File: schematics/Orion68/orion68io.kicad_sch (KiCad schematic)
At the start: 48 parts, among them IC4 XR68C681CJTR-F, J1 LevelConverter, J200 Euro96pin, J22 Kbd_usb, J23 Conn_01x06, Q4 14.7456MHz, U200 GAL16V8, U25 SN74LVC245APW, U26 SN74LVC245APW, U27 RP5C01A, U30 LM2937xT, U33 68681, Y3 Crystal

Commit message: Now picoMultiIO read usb and ps2 keyboards
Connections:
- net CS_SDCARD: now also U_S200.29 (GP22); no longer U_S200.27 (GP21)
- net TX: now reaches U_S200.26 (GP20)
- new net RX: U_S200.27 (GP21)
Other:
- moved on the sheet: J22
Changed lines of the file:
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@@
 	(wire
 		(pts
-			(xy 77.47 140.97) (xy 77.47 143.51)
+			(xy 246.38 100.33) (xy 246.38 102.87)
 		)
 		(stroke
@@
 	(wire
 		(pts
-			(xy 77.47 130.81) (xy 80.01 130.81)
+			(xy 246.38 90.17) (xy 248.92 90.17)
 		)
 		(stroke
@@
 	(wire
 		(pts
-			(xy 77.47 128.27) (xy 77.47 130.81)
+			(xy 246.38 87.63) (xy 246.38 90.17)
 		)
 		(stroke
@@
 	(wire
 		(pts
-			(xy 77.47 140.97) (xy 80.01 140.97)
+			(xy 246.38 100.33) (xy 248.92 100.33)
 		)
 		(stroke
@@
 		)
 	)
+	(label "RX"
+		(at 227.33 133.35 0)
+		(effects
+			(font
+				(size 1.27 1.27)
+			)
+			(justify left bottom)
+		)
+	)
 	(label "A20"
 		(at 391.16 59.69 0)
@@
 		)
 	)
+	(label "TX"
+		(at 227.33 135.89 0)
+		(effects
+			(font
+				(size 1.27 1.27)
+			)
+			(justify left bottom)
+		)
+	)
 	(label "{slash}DTACK_68681"
 		(at 364.49 124.46 180)
@@
 	)
 	(label "TXDA"
-		(at 80.01 138.43 180)
+		(at 248.92 97.79 180)
 		(effects
 			(font
@@
 	)
 	(label "CS_SDCARD"
-		(at 227.33 133.35 0)
+		(at 227.33 130.81 0)
 		(effects
 			(font
@@
 	)
 	(label "RXDA"
-		(at 80.01 135.89 180)
+		(at 248.92 95.25 180)
 		(effects
 			(font
@@
 	(symbol
 		(lib_id "Connector_Generic:Conn_01x05")
-		(at 85.09 135.89 0)
+		(at 254 95.25 0)
 		(unit 1)
 		(exclude_from_sim no)
@@
 		(fields_autoplaced yes)
 		(property "Reference" "J22"
-			(at 87.63 134.6199 0)
+			(at 256.54 93.9799 0)
 			(effects
 				(font
@@
 		)
 		(property "Value" "Kbd_usb"
-			(at 87.63 137.1599 0)
+			(at 256.54 96.5199 0)
 			(effects
 				(font
@@
 		)
 		(property "Footprint" ""
-			(at 85.09 135.89 0)
+			(at 254 95.25 0)
 			(effects
 				(font
@@
 		)
 		(property "Datasheet" "~"
-			(at 85.09 135.89 0)
+			(at 254 95.25 0)
 			(effects
 				(font
@@
 		)
 		(property "Description" "Generic connector, single row, 01x05, script generated (kicad-library-utils/schlib/autogen/connector/)"
-			(at 85.09 135.89 0)
+			(at 254 95.25 0)
 			(effects
 				(font
@@
 	(symbol
 		(lib_id "power:GND")
-		(at 77.47 143.51 0)
+		(at 246.38 102.87 0)
 		(unit 1)
 		(exclude_from_sim no)
@@
 		(fields_autoplaced yes)
 		(property "Reference" "#PWR0194"
-			(at 77.47 149.86 0)
+			(at 246.38 109.22 0)
 			(effects
 				(font
@@
 		)
 		(property "Value" "GND"
-			(at 77.47 148.59 0)
+			(at 246.38 107.95 0)
 			(effects
 				(font
@@
 		)
 		(property "Footprint" ""
-			(at 77.47 143.51 0)
+			(at 246.38 102.87 0)
 			(effects
 				(font
@@
 		)
 		(property "Datasheet" ""
-			(at 77.47 143.51 0)
+			(at 246.38 102.87 0)
 			(effects
 				(font
@@
 		)
 		(property "Description" "Power symbol creates a global label with name \"GND\" , ground"
-			(at 77.47 143.51 0)
+			(at 246.38 102.87 0)
 			(effects
 				(font
@@
 	(symbol
 		(lib_id "power:+5V")
-		(at 77.47 128.27 0)
+		(at 246.38 87.63 0)
 		(unit 1)
 		(exclude_from_sim no)
@@
 		(dnp no)
 		(property "Reference" "#PWR0193"
-			(at 77.47 132.08 0)
+			(at 246.38 91.44 0)
 			(effects
 				(font
@@
 		)
 		(property "Value" "+5V"
-			(at 75.438 124.714 0)
+			(at 244.348 84.074 0)
 			(effects
 				(font
@@
 		)
 		(property "Footprint" ""
-			(at 77.47 128.27 0)
+			(at 246.38 87.63 0)
 			(effects
 				(font
@@
 		)
 		(property "Datasheet" ""
-			(at 77.47 128.27 0)
+			(at 246.38 87.63 0)
 			(effects
 				(font
@@
 		)
 		(property "Description" "Power symbol creates a global label with name \"+5V\""
-			(at 77.47 128.27 0)
+			(at 246.38 87.63 0)
 			(effects
 				(font

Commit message: several code clean-ups implemented trap12
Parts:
- Q4: value 14.7456MHz -> 3.6864MHz
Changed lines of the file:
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@@
 			)
 		)
-		(property "Value" "14.7456MHz"
+		(property "Value" "3.6864MHz"
 			(at 21.59 62.8142 0)
 			(effects

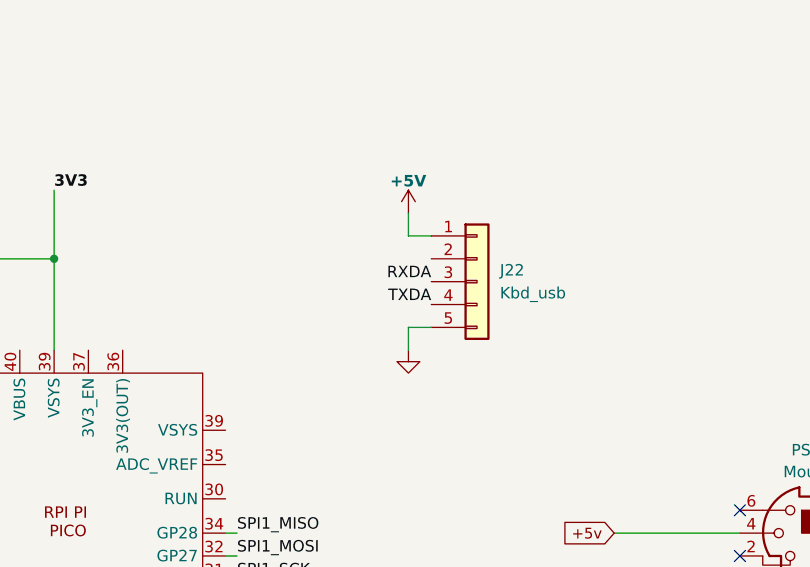
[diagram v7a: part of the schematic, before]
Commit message: RTC lib implemented missing tests
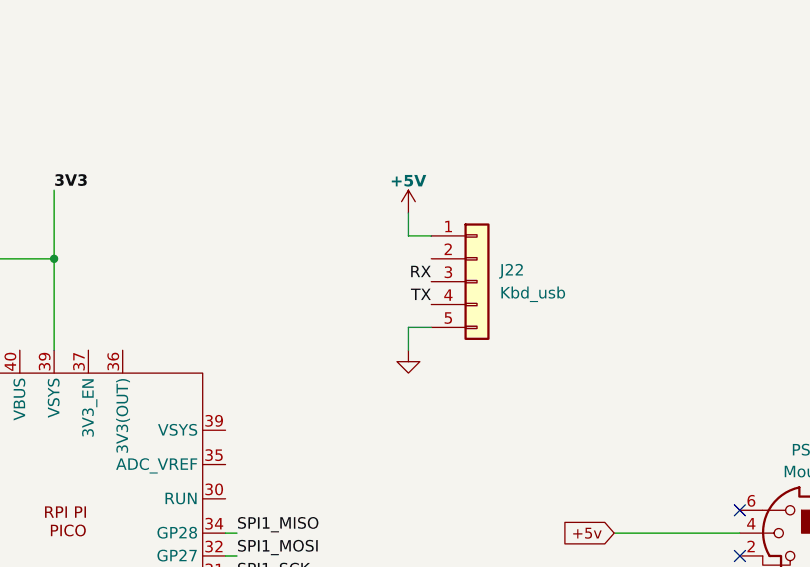
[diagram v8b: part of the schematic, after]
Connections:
- net RX: now also J22.3 (Pin_3)
- net RXDA: no longer J22.3 (Pin_3)
- net TX: now also J22.4 (Pin_4)
- net TXDA: no longer J22.4 (Pin_4)
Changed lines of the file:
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@@
+		)
+	)
+	(label "RX"
+		(at 248.92 95.25 180)
+		(effects
+			(font
+				(size 1.27 1.27)
+			)
+			(justify right bottom)
 		)
 	)
@@
 			)
 			(justify left bottom)
-		)
-	)
-	(label "TXDA"
-		(at 248.92 97.79 180)
-		(effects
-			(font
-				(size 1.27 1.27)
-			)
-			(justify right bottom)
 		)
 	)
@@
 		)
 	)
-	(label "RXDA"
-		(at 248.92 95.25 180)
-		(effects
-			(font
-				(size 1.27 1.27)
-			)
-			(justify right bottom)
-		)
-	)
 	(label "BD9"
 		(at 466.09 172.72 180)
@@
 		)
 	)
+	(label "TX"
+		(at 248.92 97.79 180)
+		(effects
+			(font
+				(size 1.27 1.27)
+			)
+			(justify right bottom)
+		)
+	)
